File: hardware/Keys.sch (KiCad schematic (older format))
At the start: 2 parts, among them U2 MCP23018_SSOP

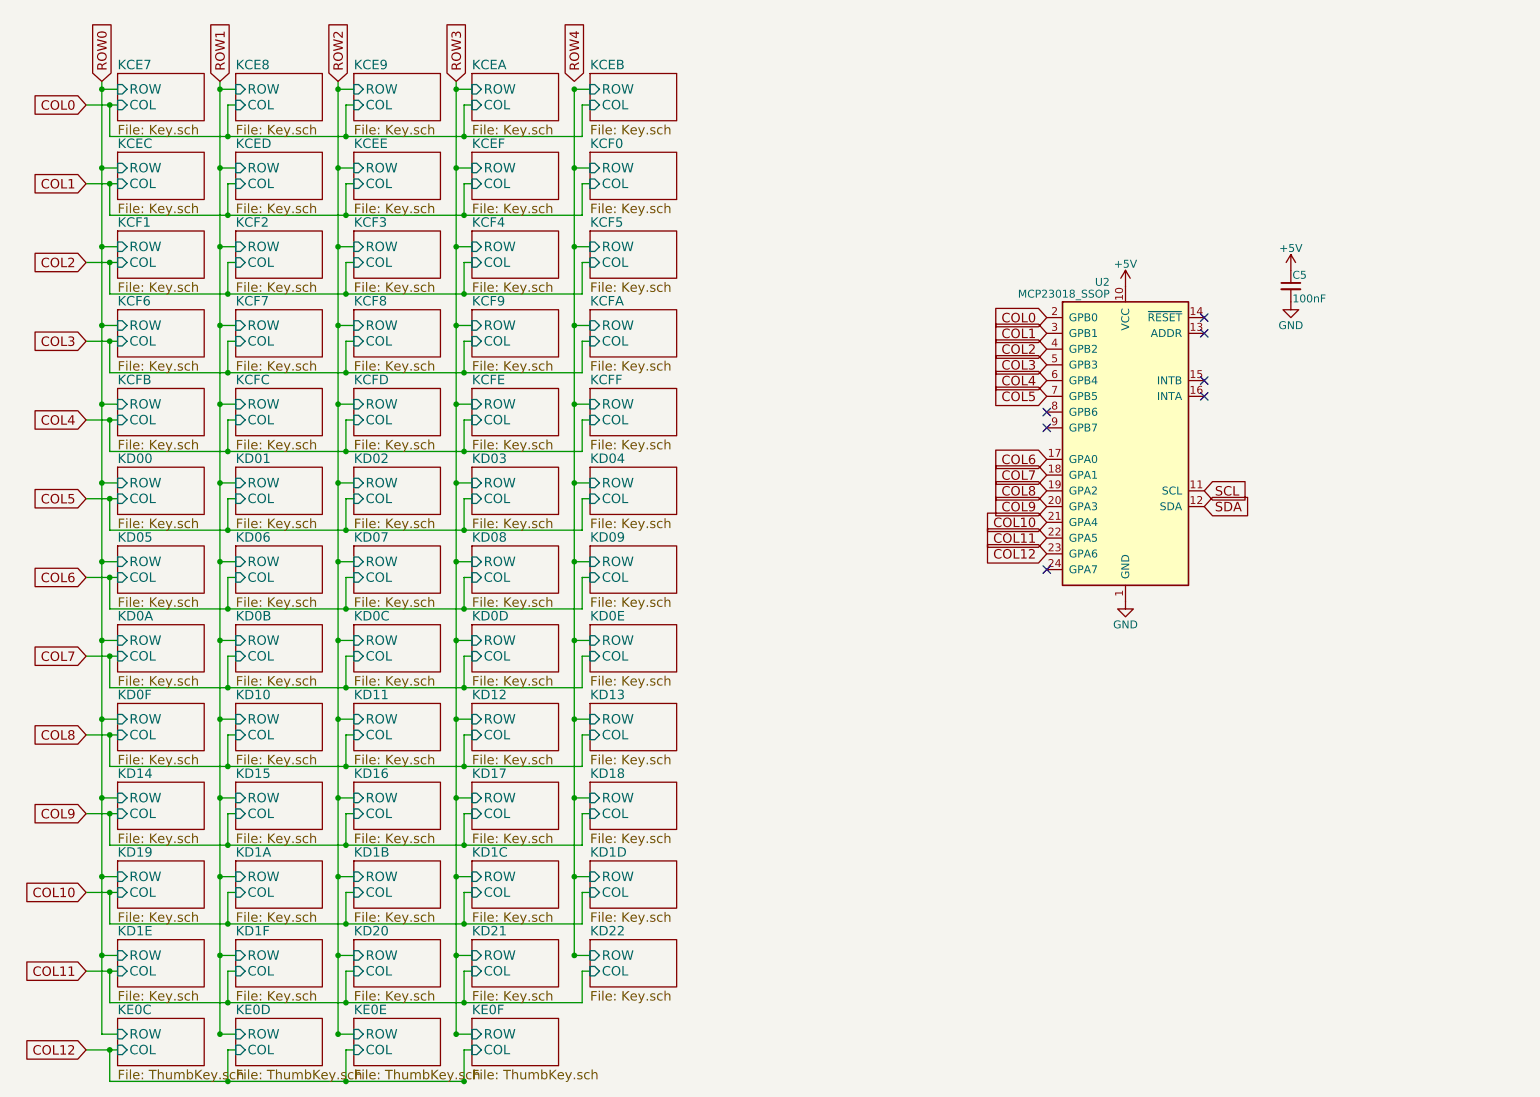
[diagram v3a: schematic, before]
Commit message: PCB revisions - more test points and fixes
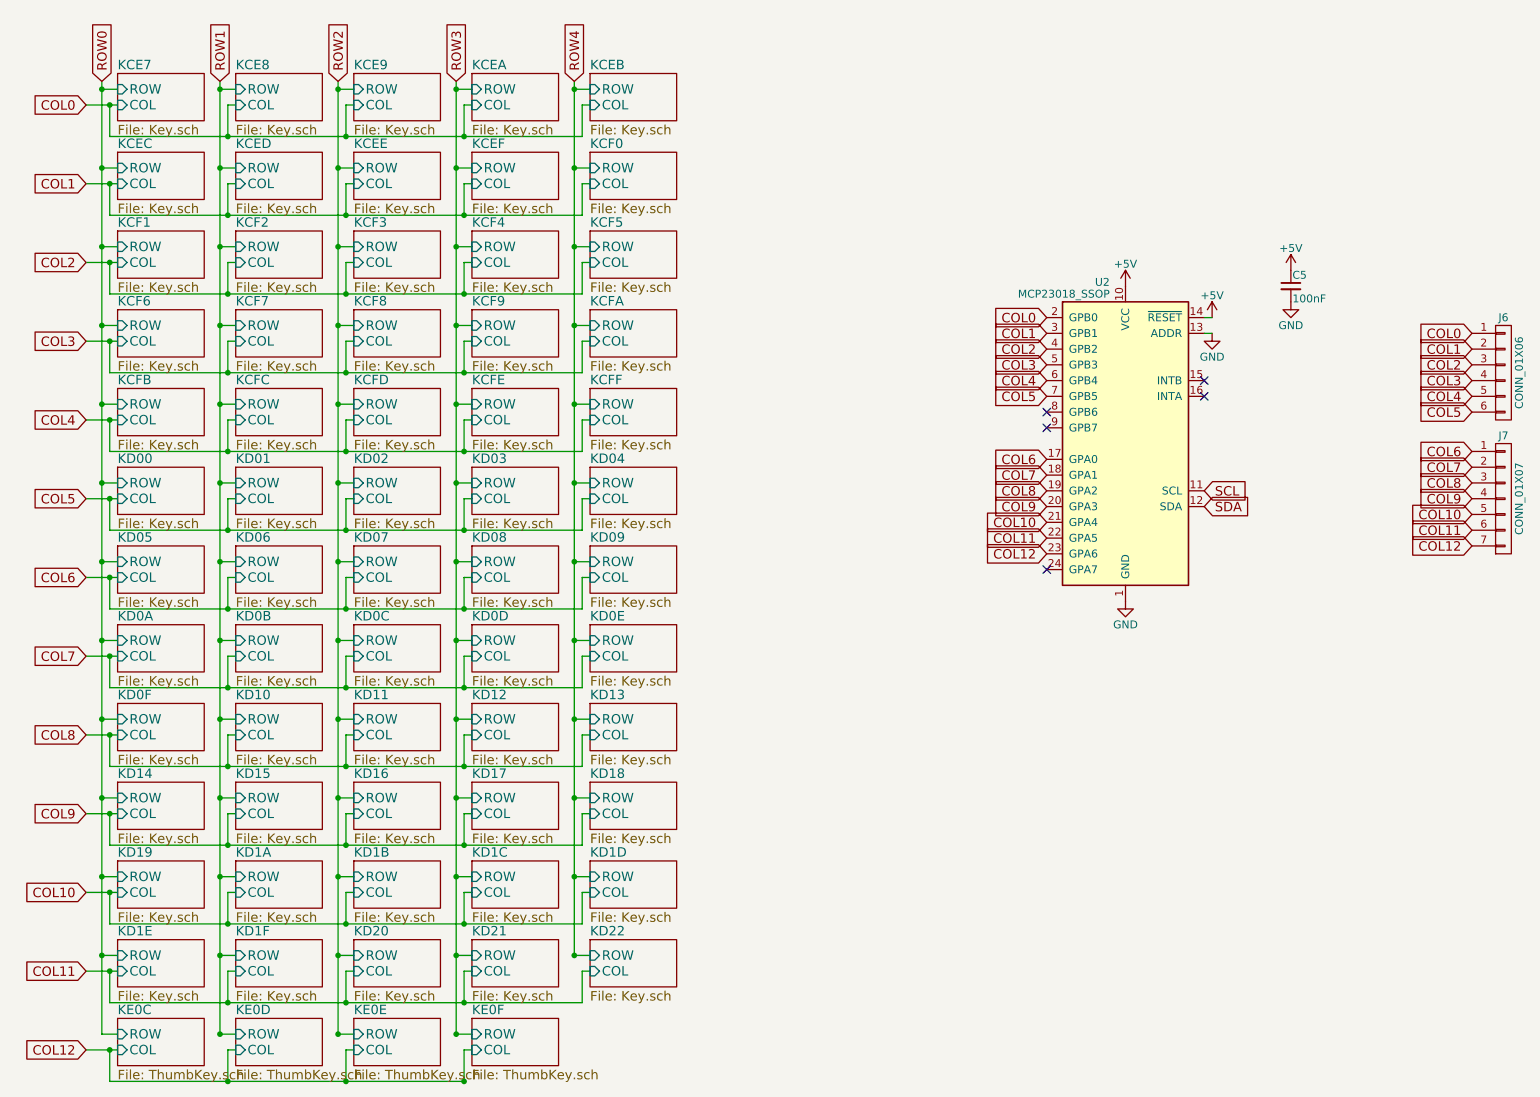
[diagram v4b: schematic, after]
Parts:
- added J6: CONN_01X06, Pin_Headers:Pin_Header_Straight_1x06_Pitch1.27mm, symbol CONN_01X06
- added J7: CONN_01X07, Pin_Headers:Pin_Header_Straight_1x07_Pitch1.27mm, symbol CONN_01X07
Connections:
- net +5V: now also U2.14 (~RESET)
- net COL0: now also J6.1 (P1)
- net COL1: now also J6.2 (P2)
- net COL10: now also J7.5 (P5)
- net COL11: now also J7.6 (P6)
- net COL12: now also J7.7 (P7)
- net COL2: now also J6.3 (P3)
- net COL3: now also J6.4 (P4)
- net COL4: now also J6.5 (P5)
- net COL5: now also J6.6 (P6)
- net COL6: now also J7.1 (P1)
- net COL7: now also J7.2 (P2)
- net COL8: now also J7.3 (P3)
- net COL9: now also J7.4 (P4)
- net GND: now also U2.13 (ADDR)
- no-connect marks 7 -> 5
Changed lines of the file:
@@
 EESchema Schematic File Version 2
-LIBS:keyboard-rescue
 LIBS:power
 LIBS:device
@@
 	1300 1000 1300 7050
 Wire Wire Line
-	4300 1050 4300 6550
+	4300 1000 4300 6550
 Text GLabel 7300 2500 0    60   Input ~ 0
 COL0
@@
 NoConn ~ 7300 4100
 $Comp
-L +5V #PWR017
+L +5V #PWR019
 U 1 1 594A3201
 P 7800 2300
-F 0 "#PWR017" H 7800 2150 50  0001 C CNN
+F 0 "#PWR019" H 7800 2150 50  0001 C CNN
 F 1 "+5V" H 7800 2440 50  0000 C CNN
 F 2 "" H 7800 2300 50  0001 C CNN
@@
 $EndComp
 $Comp
-L GND #PWR018
+L GND #PWR020
 U 1 1 594A3207
 P 7800 4300
-F 0 "#PWR018" H 7800 4050 50  0001 C CNN
+F 0 "#PWR020" H 7800 4050 50  0001 C CNN
 F 1 "GND" H 7800 4150 50  0000 C CNN
 F 2 "" H 7800 4300 50  0001 C CNN
@@
 NoConn ~ 8300 2900
 NoConn ~ 8300 3000
-NoConn ~ 8300 2500
-NoConn ~ 8300 2600
 $Comp
 L MCP23018_SSOP U2
@@
 $EndComp
 $Comp
-L +5V #PWR019
+L +5V #PWR021
 U 1 1 5955CD8D
 P 8850 2200
-F 0 "#PWR019" H 8850 2050 50  0001 C CNN
+F 0 "#PWR021" H 8850 2050 50  0001 C CNN
 F 1 "+5V" H 8850 2340 50  0000 C CNN
 F 2 "" H 8850 2200 50  0001 C CNN
@@
 $EndComp
 $Comp
-L GND #PWR020
+L GND #PWR022
 U 1 1 5955D0A5
 P 8850 2400
-F 0 "#PWR020" H 8850 2150 50  0001 C CNN
+F 0 "#PWR022" H 8850 2150 50  0001 C CNN
 F 1 "GND" H 8850 2250 50  0000 C CNN
 F 2 "" H 8850 2400 50  0001 C CNN
@@
 NoConn ~ 7300 3100
 NoConn ~ 7300 3200
+$Comp
+L CONN_01X06 J6
+U 1 1 5A2C3AEF
+P 10200 2850
+F 0 "J6" H 10200 3200 50  0000 C CNN
+F 1 "CONN_01X06" V 10300 2850 50  0000 C CNN
+F 2 "Pin_Headers:Pin_Header_Straight_1x06_Pitch1.27mm" H 10200 2850 50  0001 C CNN
+F 3 "" H 10200 2850 50  0001 C CNN
+	1    10200 2850
+	1    0    0    -1
+$EndComp
+Text GLabel 10000 2600 0    60   Input ~ 0
+COL0
+Text GLabel 10000 2700 0    60   Input ~ 0
+COL1
+Text GLabel 10000 2800 0    60   Input ~ 0
+COL2
+Text GLabel 10000 2900 0    60   Input ~ 0
+COL3
+Text GLabel 10000 3000 0    60   Input ~ 0
+COL4
+Text GLabel 10000 3100 0    60   Input ~ 0
+COL5
+$Comp
+L CONN_01X07 J7
+U 1 1 5A2C4A3F
+P 10200 3650
+F 0 "J7" H 10200 4050 50  0000 C CNN
+F 1 "CONN_01X07" V 10300 3650 50  0000 C CNN
+F 2 "Pin_Headers:Pin_Header_Straight_1x07_Pitch1.27mm" H 10200 3650 50  0001 C CNN
+F 3 "" H 10200 3650 50  0001 C CNN
+	1    10200 3650
+	1    0    0    -1
+$EndComp
+Text GLabel 10000 3350 0    60   Input ~ 0
+COL6
+Text GLabel 10000 3450 0    60   Input ~ 0
+COL7
+Text GLabel 10000 3550 0    60   Input ~ 0
+COL8
+Text GLabel 10000 3650 0    60   Input ~ 0
+COL9
+Text GLabel 10000 3750 0    60   Input ~ 0
+COL10
+Text GLabel 10000 3850 0    60   Input ~ 0
+COL11
+Text GLabel 10000 3950 0    60   Input ~ 0
+COL12
+$Comp
+L +5V #PWR023
+U 1 1 5A2C5D0E
+P 8350 2500
+F 0 "#PWR023" H 8350 2350 50  0001 C CNN
+F 1 "+5V" H 8350 2640 50  0000 C CNN
+F 2 "" H 8350 2500 50  0001 C CNN
+F 3 "" H 8350 2500 50  0001 C CNN
+	1    8350 2500
+	1    0    0    -1
+$EndComp
+$Comp
+L GND #PWR024
+U 1 1 5A2C61AE
+P 8350 2600
+F 0 "#PWR024" H 8350 2350 50  0001 C CNN
+F 1 "GND" H 8350 2450 50  0000 C CNN
+F 2 "" H 8350 2600 50  0001 C CNN
+F 3 "" H 8350 2600 50  0001 C CNN
+	1    8350 2600
+	1    0    0    -1
+$EndComp
+Wire Wire Line
+	8350 2600 8300 2600
+Wire Wire Line
+	8300 2500 8350 2500
 $EndSCHEMATC
